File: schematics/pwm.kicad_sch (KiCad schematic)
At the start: 11 parts, among them U4 LM358_DFN, U5 TL331, U6 MCP4725xxx-xCH, U7 LM358_DFN

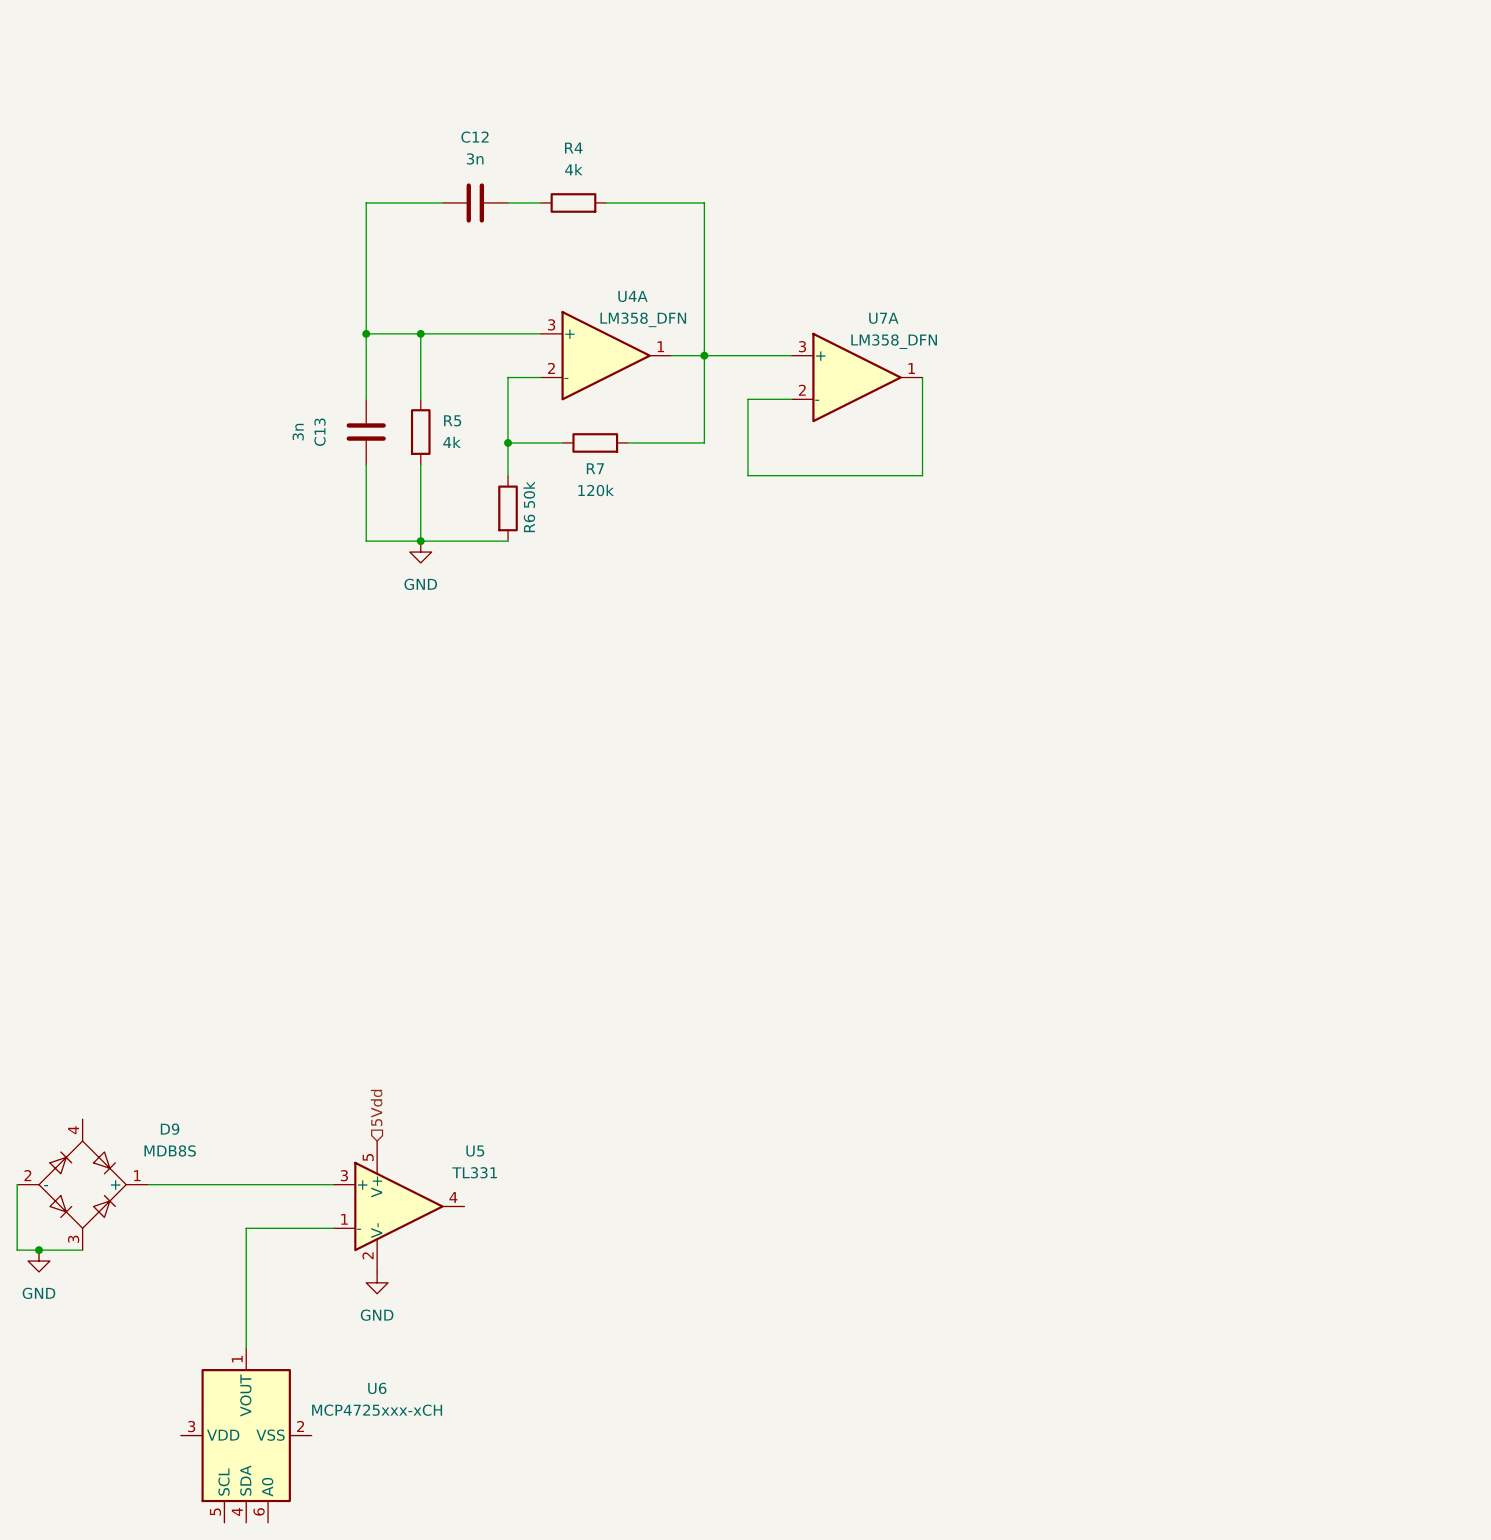
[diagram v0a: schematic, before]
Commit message: changed format to kicad project
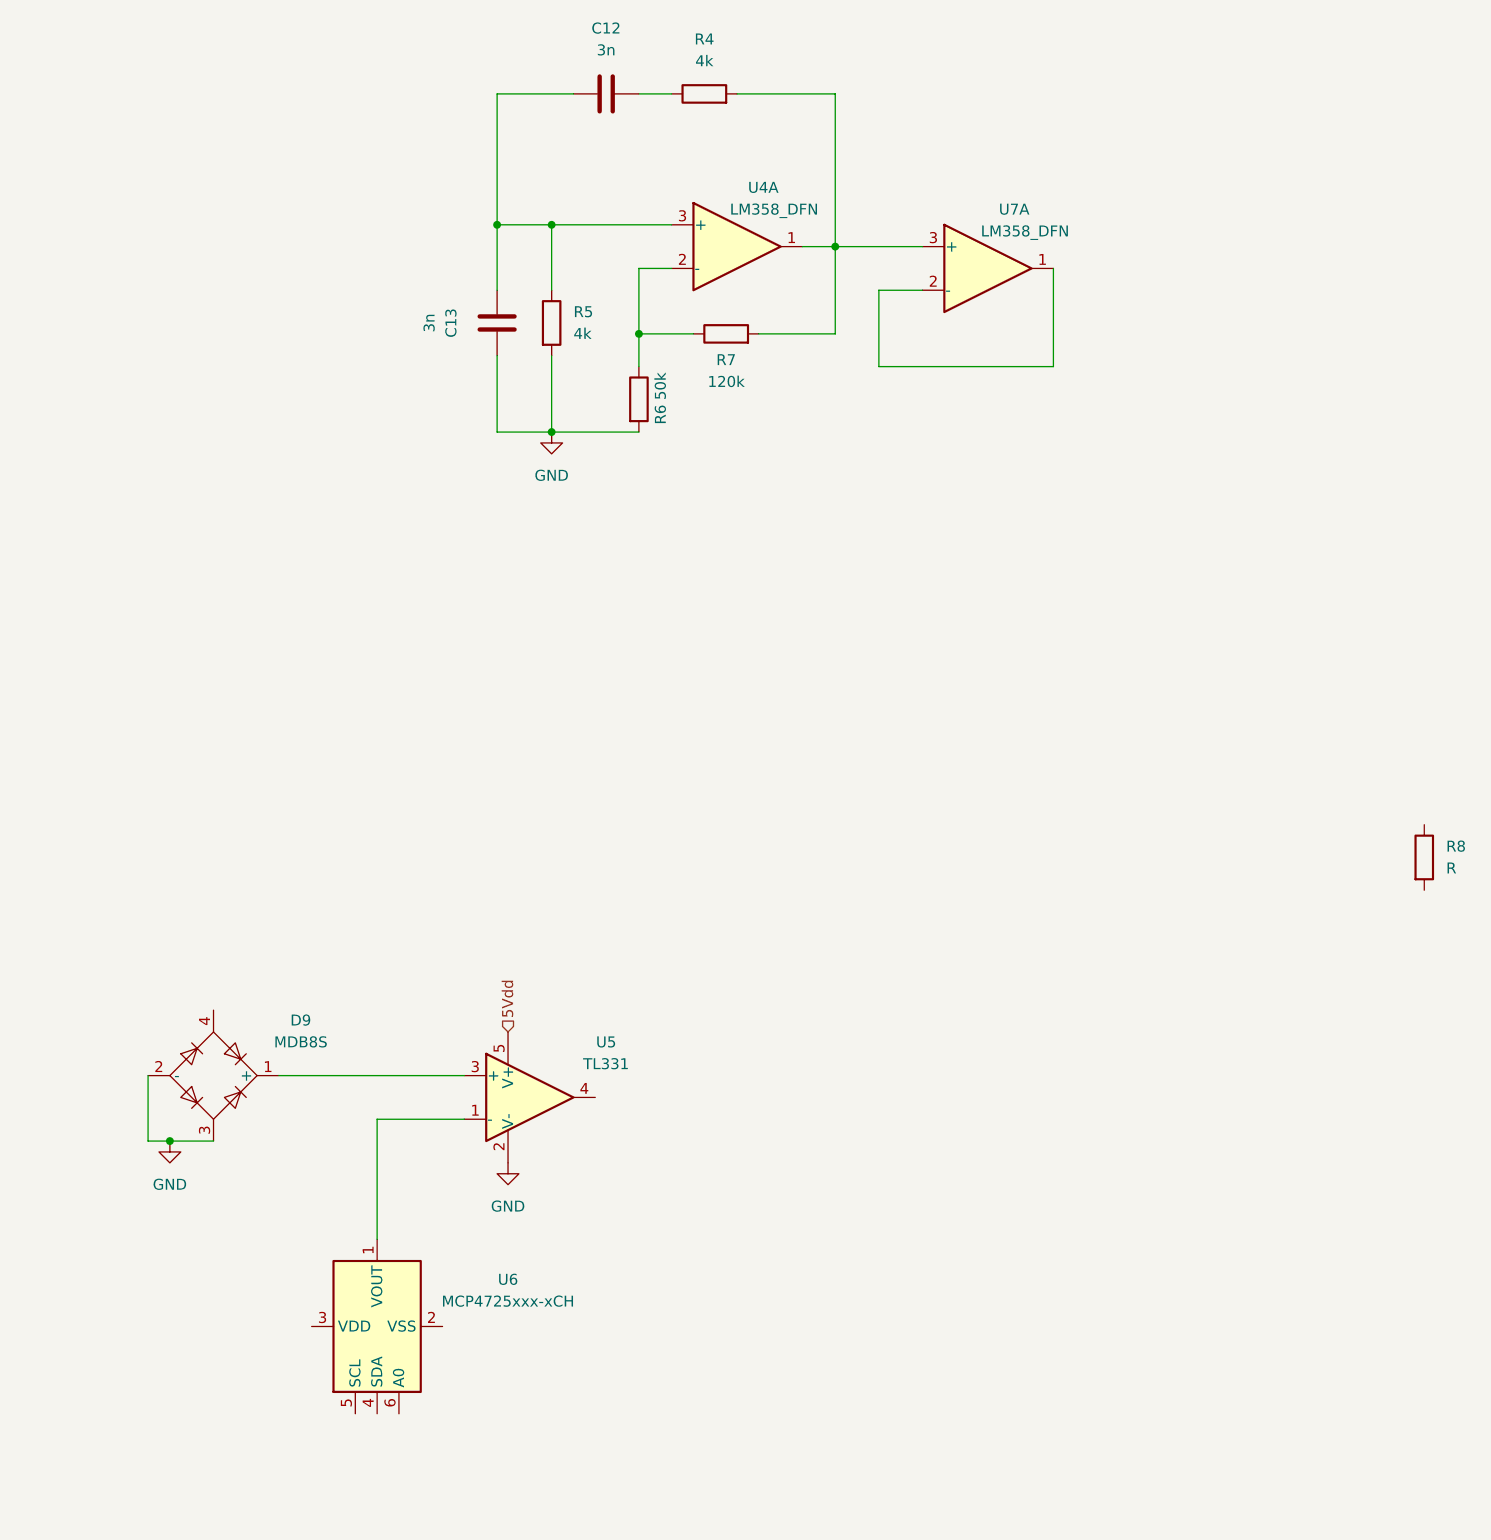
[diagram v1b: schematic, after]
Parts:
- added R8: R, symbol Device:R
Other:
- moved on the sheet: C12, C13, D9, R4, R5, R6, R7, U4A, U5, U6, U7A
